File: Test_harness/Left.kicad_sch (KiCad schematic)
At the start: 158 parts

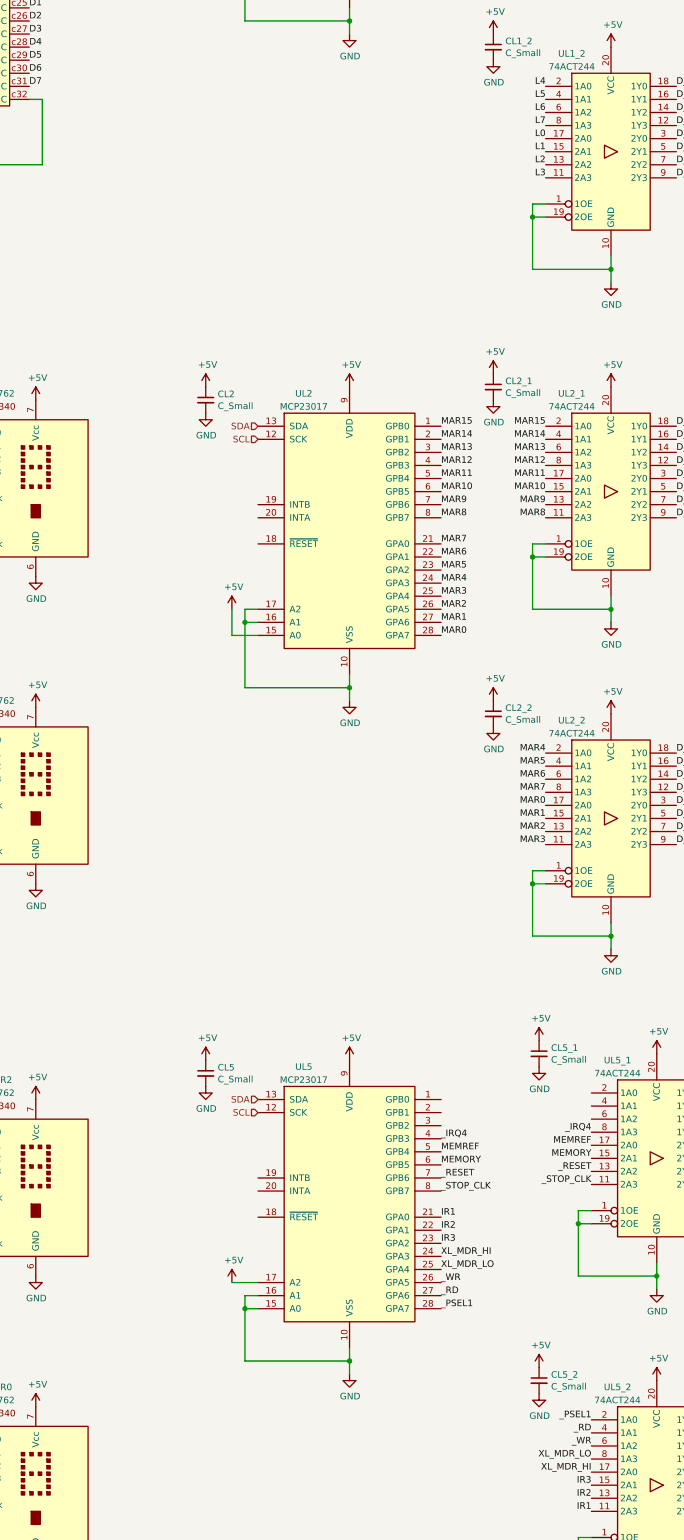
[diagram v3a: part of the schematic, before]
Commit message: fix stuff, add series resistor on clock line ohms)
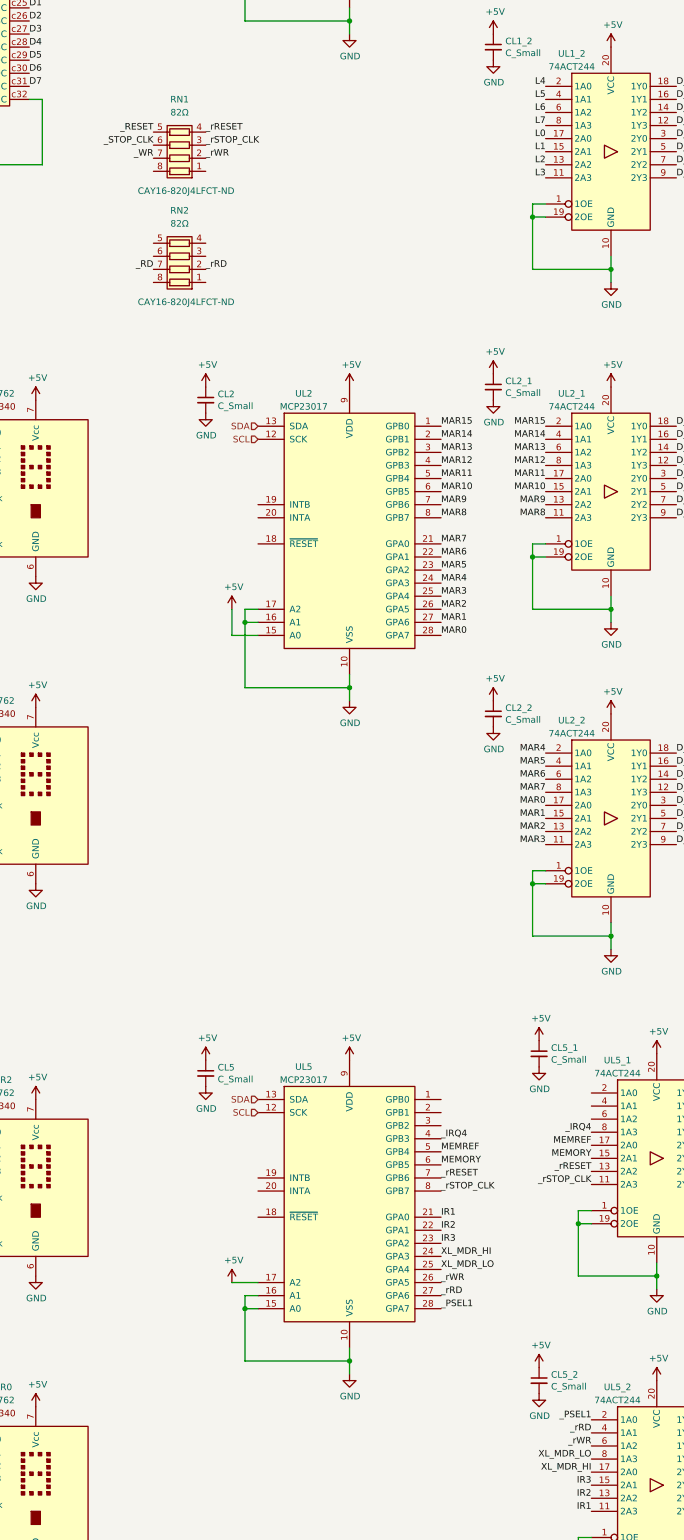
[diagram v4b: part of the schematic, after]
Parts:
- added RN1, RN2: 82Ω, Resistor_SMD:R_Array_Convex_4x1206, symbol Device:R_Pack04
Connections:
- net _RD: now also RN2.7 (R2.2); no longer UL5.27 (GPA6), UL5_2.4 (1A1)
- net _RESET: now also RN1.5 (R4.2); no longer UL5.7 (GPB6), UL5_1.13 (2A2)
- net _STOP_CLK: now also RN1.6 (R3.2); no longer UL5.8 (GPB7), UL5_1.11 (2A3)
- net _WR: now also RN1.7 (R2.2); no longer UL5.26 (GPA5), UL5_2.6 (1A2)
- new net _rRD: RN2.2 (R2.1), UL5.27 (GPA6), UL5_2.4 (1A1)
- new net _rRESET: RN1.4 (R4.1), UL5.7 (GPB6), UL5_1.13 (2A2)
- new net _rSTOP_CLK: RN1.3 (R3.1), UL5.8 (GPB7), UL5_1.11 (2A3)
- new net _rWR: RN1.2 (R2.1), UL5.26 (GPA5), UL5_2.6 (1A2)
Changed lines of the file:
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@@
   (junction (at 549.91 20.32) (diameter 1.016) (color 0 0 0 0))
   (junction (at 549.91 33.02) (diameter 1.016) (color 0 0 0 0))
-  (no_connect (at 459.74 176.53))
   (no_connect (at 457.2 176.53))
-  (no_connect (at 422.91 176.53))
   (no_connect (at 422.91 179.07))
+  (no_connect (at 422.91 176.53))
+  (no_connect (at 459.74 176.53))
   (wire (pts (xy 17.78 119.38) (xy 17.78 123.19))
     (stroke (width 0) (type solid) (color 0 0 0 0))
@@
     (effects (font (size 1.27 1.27)) (justify left bottom))
   )
+  (label "_RESET" (at 110.49 101.6 180)
+    (effects (font (size 1.27 1.27)) (justify right bottom))
+  )
+  (label "_STOP_CLK" (at 110.49 104.14 180)
+    (effects (font (size 1.27 1.27)) (justify right bottom))
+  )
+  (label "_WR" (at 110.49 106.68 180)
+    (effects (font (size 1.27 1.27)) (justify right bottom))
+  )
+  (label "_RD" (at 110.49 128.27 180)
+    (effects (font (size 1.27 1.27)) (justify right bottom))
+  )
+  (label "_rRESET" (at 120.65 101.6 0)
+    (effects (font (size 1.27 1.27)) (justify left bottom))
+  )
+  (label "_rSTOP_CLK" (at 120.65 104.14 0)
+    (effects (font (size 1.27 1.27)) (justify left bottom))
+  )
+  (label "_rWR" (at 120.65 106.68 0)
+    (effects (font (size 1.27 1.27)) (justify left bottom))
+  )
+  (label "_rRD" (at 120.65 128.27 0)
+    (effects (font (size 1.27 1.27)) (justify left bottom))
+  )
   (label "L15" (at 166.37 29.21 0)
     (effects (font (size 1.27 1.27)) (justify left bottom))
@@
     (effects (font (size 1.27 1.27)) (justify left bottom))
   )
-  (label "_RESET" (at 166.37 304.8 0)
+  (label "_rRESET" (at 166.37 304.8 0)
     (effects (font (size 1.27 1.27)) (justify left bottom))
   )
-  (label "_STOP_CLK" (at 166.37 307.34 0)
+  (label "_rSTOP_CLK" (at 166.37 307.34 0)
     (effects (font (size 1.27 1.27)) (justify left bottom))
   )
@@
     (effects (font (size 1.27 1.27)) (justify left bottom))
   )
-  (label "_WR" (at 166.37 325.12 0)
+  (label "_rWR" (at 166.37 325.12 0)
     (effects (font (size 1.27 1.27)) (justify left bottom))
   )
-  (label "_RD" (at 166.37 327.66 0)
+  (label "_rRD" (at 166.37 327.66 0)
     (effects (font (size 1.27 1.27)) (justify left bottom))
   )
@@
     (effects (font (size 1.27 1.27)) (justify right bottom))
   )
-  (label "_RESET" (at 195.58 303.53 180)
+  (label "_rRESET" (at 195.58 303.53 180)
     (effects (font (size 1.27 1.27)) (justify right bottom))
   )
-  (label "_STOP_CLK" (at 195.58 306.07 180)
+  (label "_rSTOP_CLK" (at 195.58 306.07 180)
     (effects (font (size 1.27 1.27)) (justify right bottom))
   )
@@
     (effects (font (size 1.27 1.27)) (justify right bottom))
   )
-  (label "_RD" (at 195.58 354.33 180)
+  (label "_rRD" (at 195.58 354.33 180)
     (effects (font (size 1.27 1.27)) (justify right bottom))
   )
-  (label "_WR" (at 195.58 356.87 180)
+  (label "_rWR" (at 195.58 356.87 180)
     (effects (font (size 1.27 1.27)) (justify right bottom))
   )
@@
     )
   )
+  (symbol (lib_id "Device:R_Pack04") (at 115.57 104.14 90) (unit 1)
+    (in_bom yes) (on_board yes)
+    (property "Reference" "RN1" (id 0) (at 115.57 95.25 90))
+    (property "Value" "82Ω" (id 1) (at 115.57 97.79 90))
+    (property "Footprint" "Resistor_SMD:R_Array_Convex_4x1206" (id 2) (at 115.57 97.155 90)
+      (effects (font (size 1.27 1.27)) hide)
+    )
+    (property "Datasheet" "https://www.bourns.com/docs/Product-Datasheets/CATCAY.pdf" (id 3) (at 115.57 104.14 0)
+      (effects (font (size 1.27 1.27)) hide)
+    )
+    (property "Manufacturer" "CAY16-820J4LF" (id 4) (at 115.57 104.14 90)
+      (effects (font (size 1.27 1.27)) hide)
+    )
+    (property "Digikey" "CAY16-820J4LFCT-ND" (id 5) (at 116.84 113.03 90))
+  )
+  (symbol (lib_id "Device:R_Pack04") (at 115.57 125.73 90) (unit 1)
+    (in_bom yes) (on_board yes)
+    (property "Reference" "RN2" (id 0) (at 115.57 116.84 90))
+    (property "Value" "82Ω" (id 1) (at 115.57 119.38 90))
+    (property "Footprint" "Resistor_SMD:R_Array_Convex_4x1206" (id 2) (at 115.57 118.745 90)
+      (effects (font (size 1.27 1.27)) hide)
+    )
+    (property "Datasheet" "https://www.bourns.com/docs/Product-Datasheets/CATCAY.pdf" (id 3) (at 115.57 125.73 0)
+      (effects (font (size 1.27 1.27)) hide)
+    )
+    (property "Manufacturer" "CAY16-820J4LF" (id 4) (at 115.57 125.73 90)
+      (effects (font (size 1.27 1.27)) hide)
+    )
+    (property "Digikey" "CAY16-820J4LFCT-ND" (id 5) (at 116.84 134.62 90))
+  )
   (symbol (lib_id "Device:R_Pack04") (at 241.3 49.53 0) (unit 1)

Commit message: more fixes
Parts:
- RNL2_2_1: value R_Pack04 -> 1kΩ
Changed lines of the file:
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@@
       (effects (font (size 1.27 1.27)) (justify left))
     )
-    (property "Value" "R_Pack04" (id 1) (at 245.9737 243.7193 0)
+    (property "Value" "1kΩ" (id 1) (at 245.974 243.719 0)
       (effects (font (size 1.27 1.27)) (justify left))
     )

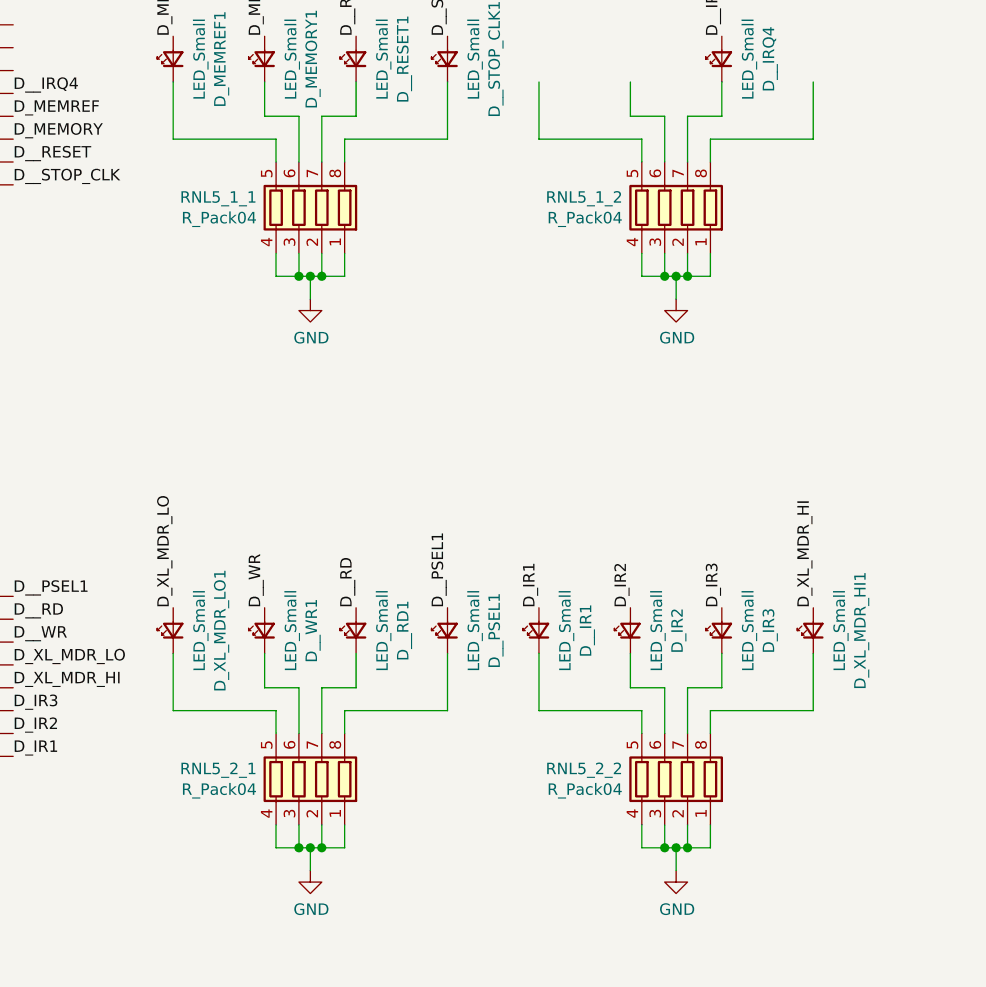
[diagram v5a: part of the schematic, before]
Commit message: position the last leds of the left side
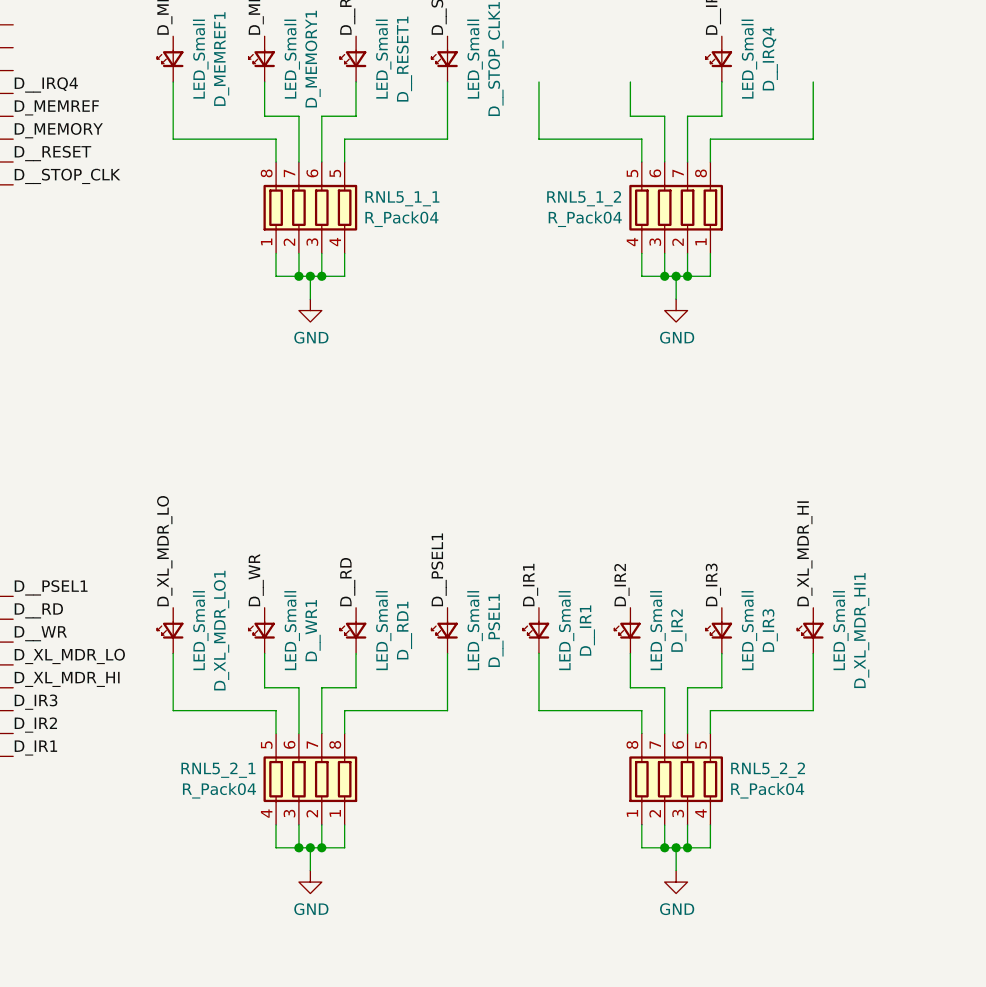
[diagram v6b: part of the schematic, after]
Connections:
- net at RNL5_2_2.5 (R4.2): now also D_XL_MDR_HI1.1 (K); no longer D__IR1.1 (K)
- net at RNL5_2_2.6 (R3.2): now also D_IR3.1 (K); no longer D_IR2.1 (K)
- net at RNL5_2_2.7 (R2.2): now also D_IR2.1 (K); no longer D_IR3.1 (K)
- net at RNL5_2_2.8 (R1.2): now also D__IR1.1 (K); no longer D_XL_MDR_HI1.1 (K)
- net at RNL5_1_1.5 (R4.2): now also D__STOP_CLK1.1 (K); no longer D_MEMREF1.1 (K)
- net at RNL5_1_1.6 (R3.2): now also D__RESET1.1 (K); no longer D_MEMORY1.1 (K)
- net at RNL5_1_1.7 (R2.2): now also D_MEMORY1.1 (K); no longer D__RESET1.1 (K)
- net at RNL5_1_1.8 (R1.2): now also D_MEMREF1.1 (K); no longer D__STOP_CLK1.1 (K)
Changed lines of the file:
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@@
-    )
-  )
-  (symbol (lib_id "Device:R_Pack04") (at 252.73 308.61 0) (mirror y) (unit 1)
-    (in_bom yes) (on_board yes)
-    (property "Reference" "RNL5_1_1" (id 0) (at 248.056 307.461 0)
-      (effects (font (size 1.27 1.27)) (justify left))
-    )
-    (property "Value" "R_Pack04" (id 1) (at 248.0563 309.7593 0)
-      (effects (font (size 1.27 1.27)) (justify left))
-    )
-    (property "Footprint" "Resistor_SMD:R_Array_Convex_4x1206" (id 2) (at 245.745 308.61 90)
-      (effects (font (size 1.27 1.27)) hide)
-    )
-    (property "Datasheet" "~" (id 3) (at 252.73 308.61 0)
-      (effects (font (size 1.27 1.27)) hide)
-    )
-    (property "Manufacturer" "CAY16-331J4LF" (id 4) (at 252.73 308.61 0)
-      (effects (font (size 1.27 1.27)) hide)
-    )
-    (property "Digikey" "CAY16-331J4LFCT-ND" (id 5) (at 252.73 308.61 0)
-      (effects (font (size 1.27 1.27)) hide)
     )
   )
@@
     )
     (property "Digikey" "CAY16-331J4LFCT-ND" (id 5) (at 252.73 372.11 0)
+      (effects (font (size 1.27 1.27)) hide)
+    )
+  )
+  (symbol (lib_id "Device:R_Pack04") (at 255.27 308.61 0) (unit 1)
+    (in_bom yes) (on_board yes)
+    (property "Reference" "RNL5_1_1" (id 0) (at 259.944 307.461 0)
+      (effects (font (size 1.27 1.27)) (justify left))
+    )
+    (property "Value" "R_Pack04" (id 1) (at 259.9437 309.7593 0)
+      (effects (font (size 1.27 1.27)) (justify left))
+    )
+    (property "Footprint" "Resistor_SMD:R_Array_Convex_4x1206" (id 2) (at 262.255 308.61 90)
+      (effects (font (size 1.27 1.27)) hide)
+    )
+    (property "Datasheet" "~" (id 3) (at 255.27 308.61 0)
+      (effects (font (size 1.27 1.27)) hide)
+    )
+    (property "Manufacturer" "CAY16-331J4LF" (id 4) (at 255.27 308.61 0)
+      (effects (font (size 1.27 1.27)) hide)
+    )
+    (property "Digikey" "CAY16-331J4LFCT-ND" (id 5) (at 255.27 308.61 0)
       (effects (font (size 1.27 1.27)) hide)
     )
@@
     )
   )
-  (symbol (lib_id "Device:R_Pack04") (at 293.37 372.11 0) (mirror y) (unit 1)
+  (symbol (lib_id "Device:R_Pack04") (at 295.91 372.11 0) (unit 1)
     (in_bom yes) (on_board yes)
-    (property "Reference" "RNL5_2_2" (id 0) (at 288.696 370.961 0)
+    (property "Reference" "RNL5_2_2" (id 0) (at 300.584 370.961 0)
       (effects (font (size 1.27 1.27)) (justify left))
     )
-    (property "Value" "R_Pack04" (id 1) (at 288.6963 373.2593 0)
+    (property "Value" "R_Pack04" (id 1) (at 300.5837 373.2593 0)
       (effects (font (size 1.27 1.27)) (justify left))
     )
-    (property "Footprint" "Resistor_SMD:R_Array_Convex_4x1206" (id 2) (at 286.385 372.11 90)
+    (property "Footprint" "Resistor_SMD:R_Array_Convex_4x1206" (id 2) (at 302.895 372.11 90)
       (effects (font (size 1.27 1.27)) hide)
     )
-    (property "Datasheet" "~" (id 3) (at 293.37 372.11 0)
+    (property "Datasheet" "~" (id 3) (at 295.91 372.11 0)
       (effects (font (size 1.27 1.27)) hide)
     )
-    (property "Digikey" "CAY16-331J4LFCT-ND" (id 4) (at 293.37 372.11 0)
+    (property "Digikey" "CAY16-331J4LFCT-ND" (id 4) (at 295.91 372.11 0)
       (effects (font (size 1.27 1.27)) hide)
     )
-    (property "Manufacturer" "CAY16-331J4LF" (id 5) (at 293.37 372.11 0)
+    (property "Manufacturer" "CAY16-331J4LF" (id 5) (at 295.91 372.11 0)
       (effects (font (size 1.27 1.27)) hide)
     )

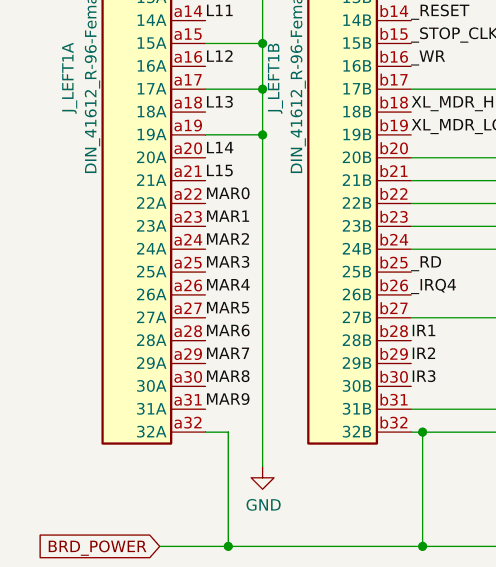
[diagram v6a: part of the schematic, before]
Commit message: change all caps to 0805
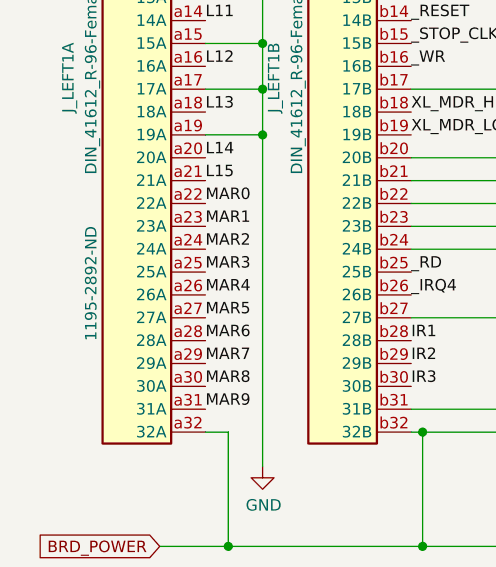
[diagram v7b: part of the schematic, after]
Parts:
- J_LEFT1: Digikey (none) -> 1195-2892-ND
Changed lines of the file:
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@@
   (junction (at 549.91 20.32) (diameter 1.016) (color 0 0 0 0))
   (junction (at 549.91 33.02) (diameter 1.016) (color 0 0 0 0))
-  (no_connect (at 457.2 176.53))
+  (no_connect (at 459.74 176.53))
   (no_connect (at 422.91 179.07))
+  (no_connect (at 457.2 176.53))
   (no_connect (at 422.91 176.53))
-  (no_connect (at 459.74 176.53))
   (wire (pts (xy 17.78 119.38) (xy 17.78 123.19))
     (stroke (width 0) (type solid) (color 0 0 0 0))
@@
       (effects (font (size 1.27 1.27)) hide)
     )
+    (property "Digikey" "1195-2892-ND" (id 4) (at 20.32 78.74 90))
   )
   (symbol (lib_id "DIN_41612:DIN_41612_C-96") (at 48.26 55.88 0) (mirror y) (unit 2)
